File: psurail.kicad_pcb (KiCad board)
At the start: 2 copper layers, 250 x 35 mm, 20 parts, among them J1 Conn_02x05_Odd_Even, J10 Conn_02x05_Odd_Even, J2 Conn_02x05_Odd_Even, J3 Conn_02x05_Odd_Even, J4 Conn_02x05_Odd_Even, J5 Conn_02x05_Odd_Even, J6 Conn_02x05_Odd_Even, J7 Conn_02x05_Odd_Even, J8 Conn_02x05_Odd_Even, J9 Conn_02x05_Odd_Even

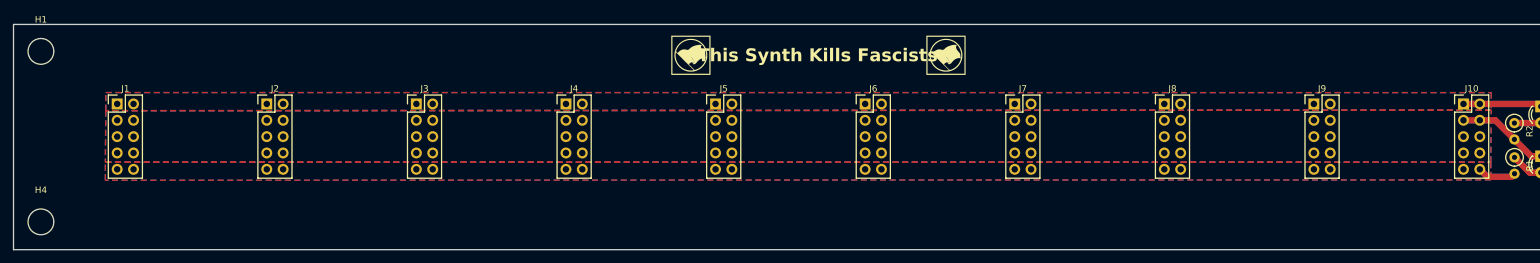
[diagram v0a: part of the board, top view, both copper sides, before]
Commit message: Updated footprint for headers
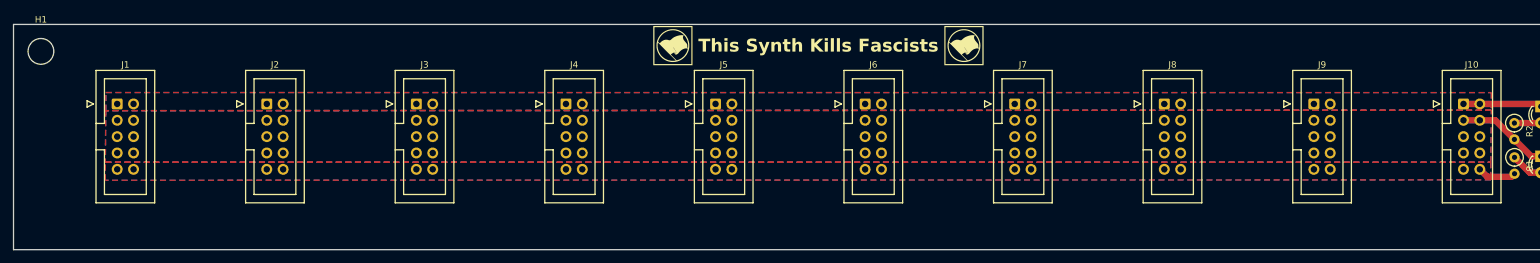
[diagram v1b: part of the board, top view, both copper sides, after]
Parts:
- removed H4: MountingHole, MountingHole:MountingHole_4mm
- removed the REF** at (167.6, 25.2)
- removed the REF** at (128.0, 25.2)
- added REF**: black_flag, eurorack_frontpanel_biondo:black_flag, F.Cu at (170.4, 23.7)
- added REF**: black_flag, eurorack_frontpanel_biondo:black_flag, F.Cu at (125.2, 23.7)
- J1, J10, J2, J3, J4, J5, J6, J7, J8, J9: footprint Connector_PinHeader_2.54mm:PinHeader_2x05_P2.54mm_Vertical -> Connector_IDC:IDC-Header_2x05_P2.54mm_Vertical
